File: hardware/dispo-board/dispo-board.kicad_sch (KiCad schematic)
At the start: 32 parts, among them SW1 SW_Push, U1 TPS79633DCQ, U2 STM32H725RGV6, Y1 32M

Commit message: error in schematic: no LDO on package, must use SMPS, switched to kicad 8, modified filter script
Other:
- note added: "Note PWR: Use internal LDO regulator (Config 1) IMPORTANT NOTE: No LDO on 68PIN PACKAGE!!"
- note removed: "Note PWR: Use internal LDO regulator (Config 1)"
- note removed: "look up: vcap pins connected?"
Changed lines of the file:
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@@
-(kicad_sch (version 20230121) (generator eeschema)
-  (paper "A4")
+(kicad_sch
+	(version 20231120)
+	(generator "eeschema")
+	(generator_version "8.0")
+	(paper "A4")

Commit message: schematic should be ready, changed parts, ...
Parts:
- removed C11, C18: 2u2, Capacitor_SMD:C_0603_1608Metric, symbol Device:C
- removed C13, C17: 1u, Capacitor_SMD:C_0603_1608Metric, symbol Device:C
- removed C14, C8: 10n, Capacitor_SMD:C_0402_1005Metric, symbol Device:C
- removed C3, C4, C5, C6: 100n, Capacitor_SMD:C_0402_1005Metric, symbol Device:C
- removed D3: LED power, LED_SMD:LED_0603_1608Metric, symbol Device:LED
- removed FB1: 120R, Resistor_SMD:R_0402_1005Metric, symbol Device:FerriteBead
- removed R1: 180, Resistor_SMD:R_0603_1608Metric, symbol Device:R
- removed SW1: SW_Push, Button_Switch_SMD:SW_Push_1P1T_NO_6x6mm_H9.5mm, symbol Switch:SW_Push
- removed U1: TPS79633DCQ, Package_TO_SOT_SMD:SOT-223-6, symbol MySymbols:TPS79633DCQ
- removed U2: STM32H725RGV6, Package_DFN_QFN:QFN-68-1EP_8x8mm_P0.4mm_EP6.4x6.4mm, symbol MCU_ST_STM32H7:STM32H725RGVx
- added C24: 1u, Capacitor_SMD:C_0402_1005Metric, symbol Device:C
- added C30, C31, C35, C42, C43, C44: 100n, Capacitor_SMD:C_0402_1005Metric, symbol Device:C
- added SW2: SW_Push, Button_Switch_SMD:SW_Push_1P1T_NO_CK_KSC7xxJ, symbol Switch:SW_Push
- added U7: STM32H725RGVx, Package_DFN_QFN:QFN-68-1EP_8x8mm_P0.4mm_EP6.4x6.4mm, symbol MCU_ST_STM32H7:STM32H725RGVx
- C1, C2: value 100n -> 1u; MOUSER_NR 81-GRM15R61A104KA01J -> 963-LMK105BJ105MVHF
- C10, C9: value 1u -> 100n; footprint Capacitor_SMD:C_0603_1608Metric -> Capacitor_SMD:C_0402_1005Metric; MOUSER_NR 81-GRM185R61C105KE4J -> 963-MCASL105SB7104KF
- C12: MOUSER_NR 81-GRM15R61A104KA01J -> 963-MCASL105SB7104KF
- C15, C16: MOUSER_NR 81-GRM1555C1H160GA1D -> 81-GCM1555C1H160FA6D
- C19: value 2u2 -> 100n; footprint Capacitor_SMD:C_0603_1608Metric -> Capacitor_SMD:C_0402_1005Metric; MOUSER_NR 81-GRM188R71A225KE5J -> 963-MCASL105SB7104KF
- C7: MOUSER_NR 81-GRM188C81A106MA3D -> 963-LMK107BBJ106MALT
- D1: value LED power -> LED Status 1; MOUSER_NR 645-598-8N80-107F -> 645-598-8N80-107F
- D2: value LED power -> LED Status 2; MOUSER_NR 645-598-8N80-107F -> 645-598-8N80-107F
- R2, R5: MOUSER_NR 71-CRCW040210K0FKEDC -> 652-CR0402-JW-103GLF
- R3, R4: value 180 -> 220; footprint Resistor_SMD:R_0603_1608Metric -> (none); MOUSER_NR 652-CR0603JW-181ELF -> 652-CR0402FX-2200GLF
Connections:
- net +3.3VA: now also U7.16 (VDDA); no longer C9.1
- net +3V3: now also C19.1, C9.1, D1.2 (A), C30.1, C31.1, U7.1 (VBAT), U7.22 (VDD), U7.35 (VDD), U7.51 (VDD), U7.68 (VDD), U7.9 (VDD); no longer C1.1, C2.1
- net ADC1_INP4: now also U7.27 (PC4)
- net ADC1_INP5: now also U7.30 (PB1)
- net ADC1_INP8: now also U7.28 (PC5)
- net DIG_IN1: now also U7.54 (PC10)
- net DIG_IN2: now also U7.55 (PC11)
- net DIG_IN3: now also U7.56 (PC12)
- net DIG_IN4: now also U7.57 (PD2)
- net GND: now also C24.2, C30.2, C31.2, C35.2, C42.2, C43.2, C44.2, SW2.2, U7.15 (VSSA), U7.21 (VSS), U7.34 (VSS), U7.4 (VSSSMPS), U7.50 (VSS), U7.6 (VDDSMPS), U7.67 (VSS), U7.69 (VSS), U7.7 (VFBSMPS), U7.8 (VSS); no longer D1.1 (K)
- net HSE_IN: now also U7.10 (PH0)
- net HSE_OUT: now also U7.11 (PH1)
- net I2C1_SCL: now also U7.64 (PB8)
- net I2C1_SDA: now also U7.62 (PB7)
- net I2S6_CK: now also U7.24 (PA5)
- net I2S6_MCK: now also U7.20 (PA3)
- net I2S6_SDI: now also U7.25 (PA6)
- net I2S6_SDO: now also U7.26 (PA7)
- net I2S6_WS: now also U7.23 (PA4)
- net LED_STATUS1: now also U7.38 (PB14)
- net LED_STATUS2: now also U7.39 (PB15)
- net NRST: now also C2.1, SW2.1, U7.12 (NRST)
- net SWCLK: now also U7.52 (PA14(JTCK)
- net SWDIO: now also U7.48 (PA13(JTMS)
- net SWO: now also U7.58 (PB3(JTDO)
- net USBD+: now also U7.47 (PA12)
- net USBD-: now also U7.46 (PA11)
- net at R4.1: now also D2.1 (K)
- net at R3.1: now also D1.1 (K); no longer D2.1 (K)
- net at R2.1: now also U7.63 (BOOT0)
- new net +1V0: C1.1, C24.1, C35.1, C42.1, C43.1, C44.1, U7.33 (VCAP), U7.49 (VCAP), U7.66 (VCAP)
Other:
- added sheet power (power.kicad_sch)
- note added: "V_Core Decoupling"
- note removed: "- 0.5mm trace"
- note removed: "Note PWR: Use internal LDO regulator (Config 1) IMPORTANT NOTE: No LDO on 68PIN PACKAGE!!"
- note removed: "Power"
- moved on the sheet: C15, C7, R5, Y1
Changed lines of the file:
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@@
 (kicad_sch
-	(version 20231120)
+	(version 20250114)
 	(generator "eeschema")
-	(generator_version "8.0")
+	(generator_version "9.0")
 	(paper "A4")

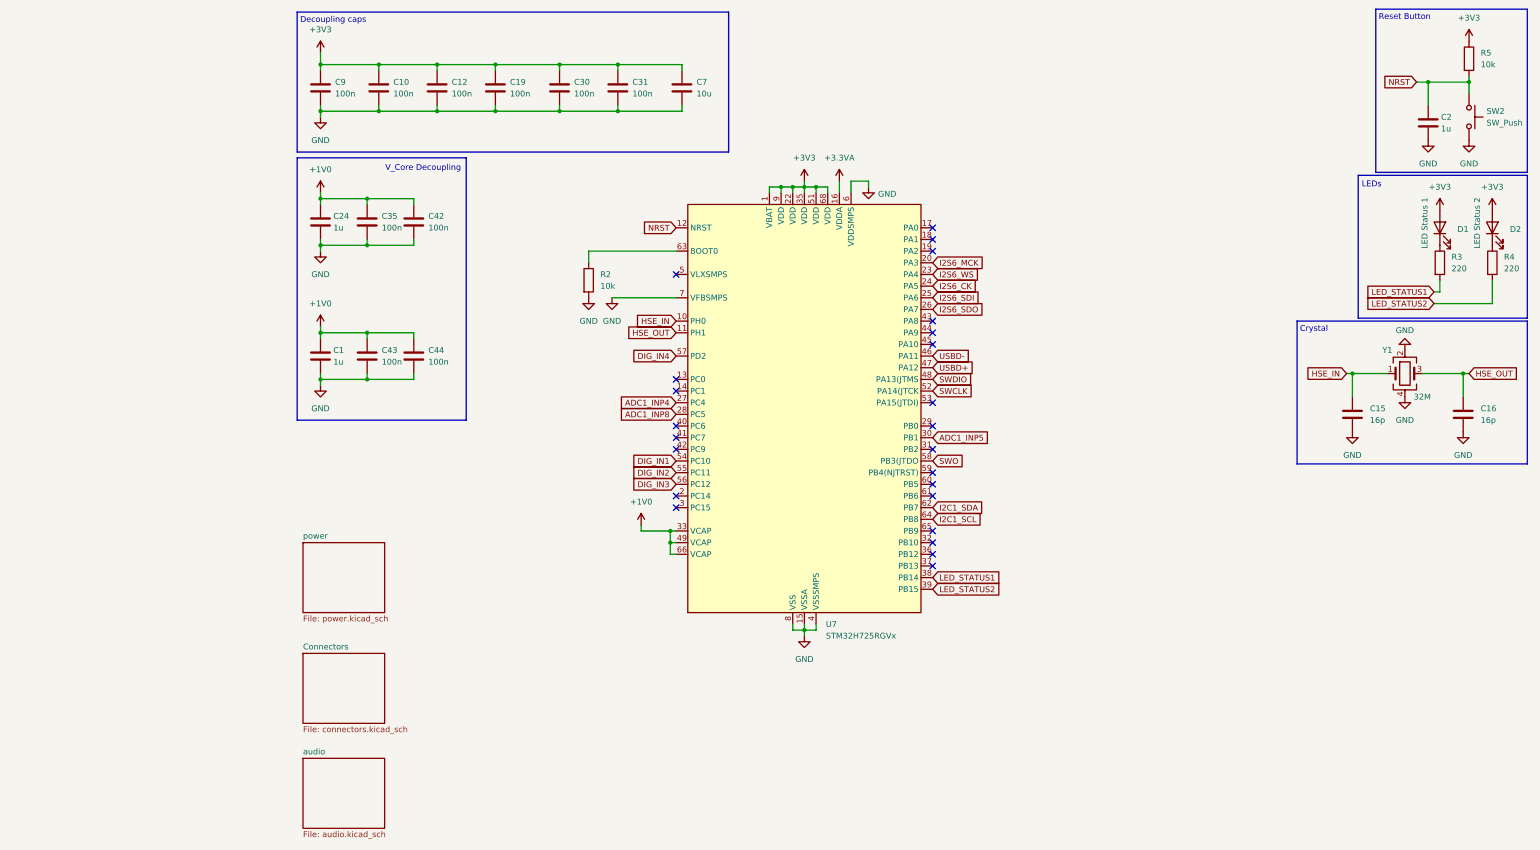
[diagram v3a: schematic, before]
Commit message: deleted nucleo board files, schematic ready?, changed to usb c
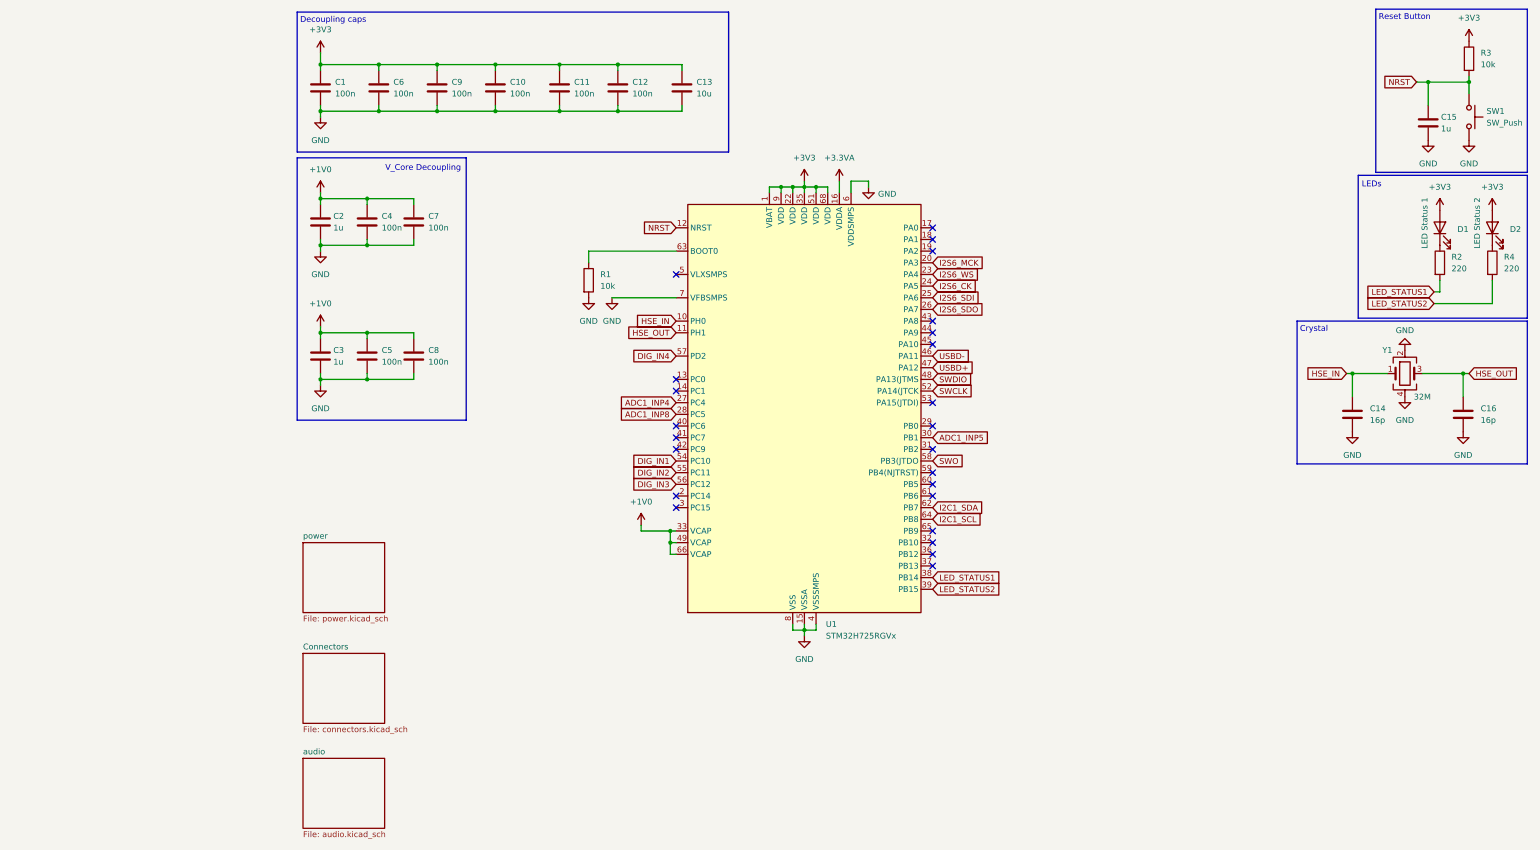
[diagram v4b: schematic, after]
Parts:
- R2: renamed from R3; footprint (none) -> Resistor_SMD:R_0402_1005Metric
- R4: footprint (none) -> Resistor_SMD:R_0402_1005Metric
- renumbered C9 to C1, C19 to C10, C30 to C11, C31 to C12, C7 to C13, C15 to C14, C2 to C15, C24 to C2, C1 to C3, C35 to C4, C43 to C5, C10 to C6, C42 to C7, C44 to C8, C12 to C9, R2 to R1, R5 to R3, SW2 to SW1, U7 to U1

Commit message: ordered pcb and stuff
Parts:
- C14: MOUSER_NR 81-GCM1555C1H160FA6D -> 81-GRT1555C1H160FA2D
- U1: MOUSER_NR (none) -> 511-STM32H725RGV6
